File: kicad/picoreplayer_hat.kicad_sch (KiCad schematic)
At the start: 20 parts, among them J1 5v IN, J2 PANEL ON/OFF, J3 Raspberry_Pi3, J4 DISPLAY, J5 DAC, J6 PICORE ENCODER & BTN, K2 Relay_HFD2_bistabile, Q1 2N3904, Q2 2N3904, SW1 ON/OFF, SW2 HARD STOP

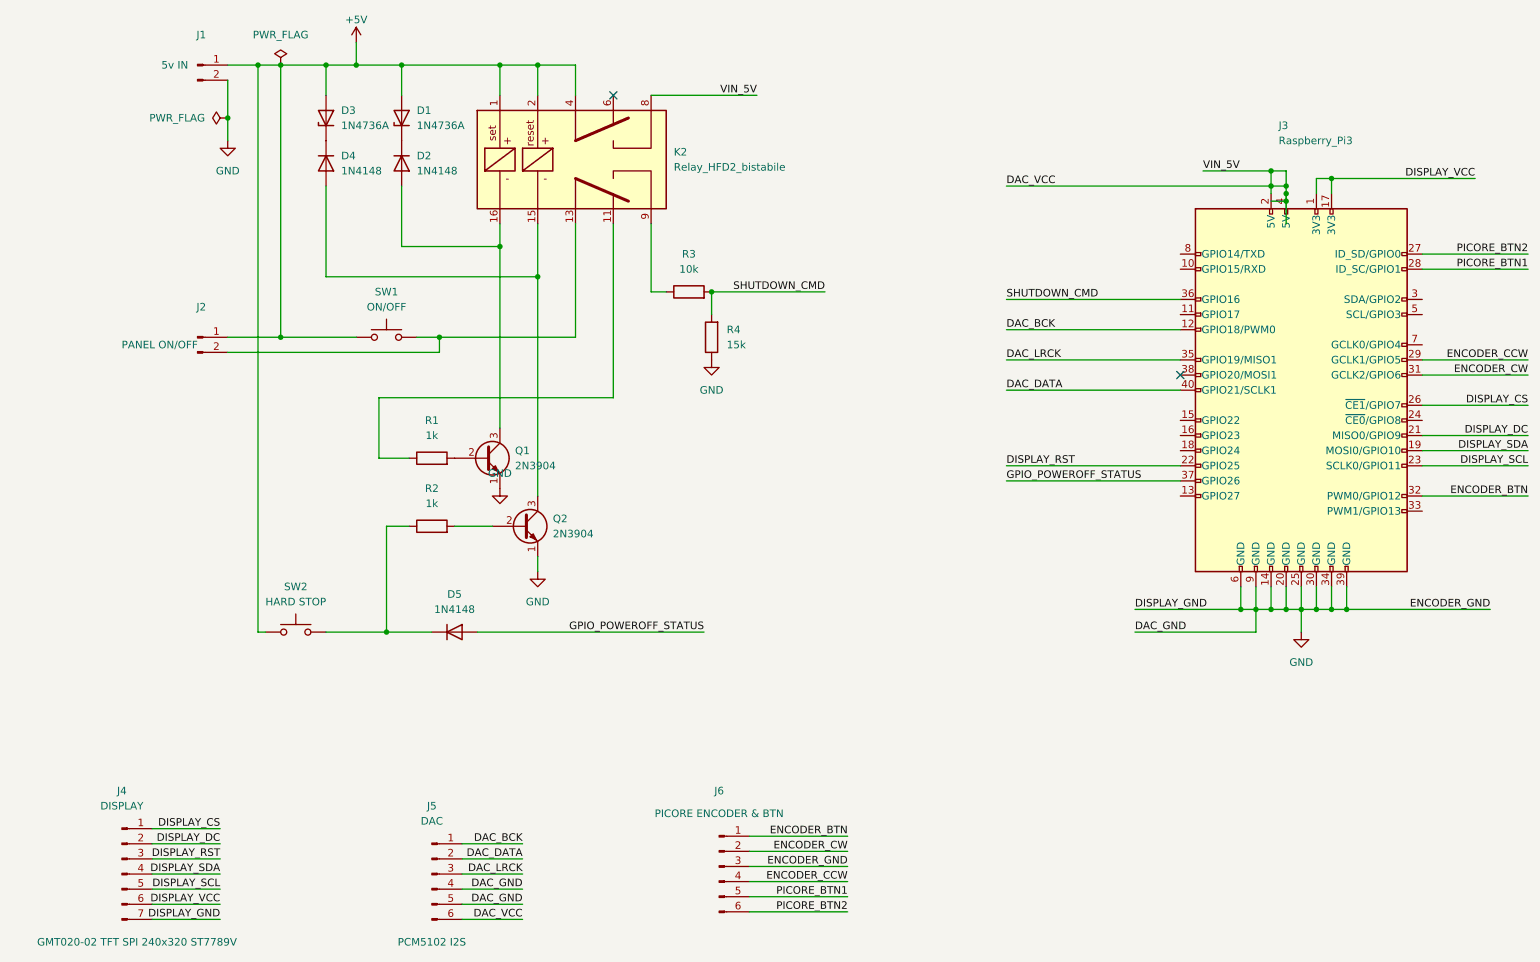
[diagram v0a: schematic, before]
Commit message: changed diode model to 1N4007 and added pulldown resistors to the transistor base
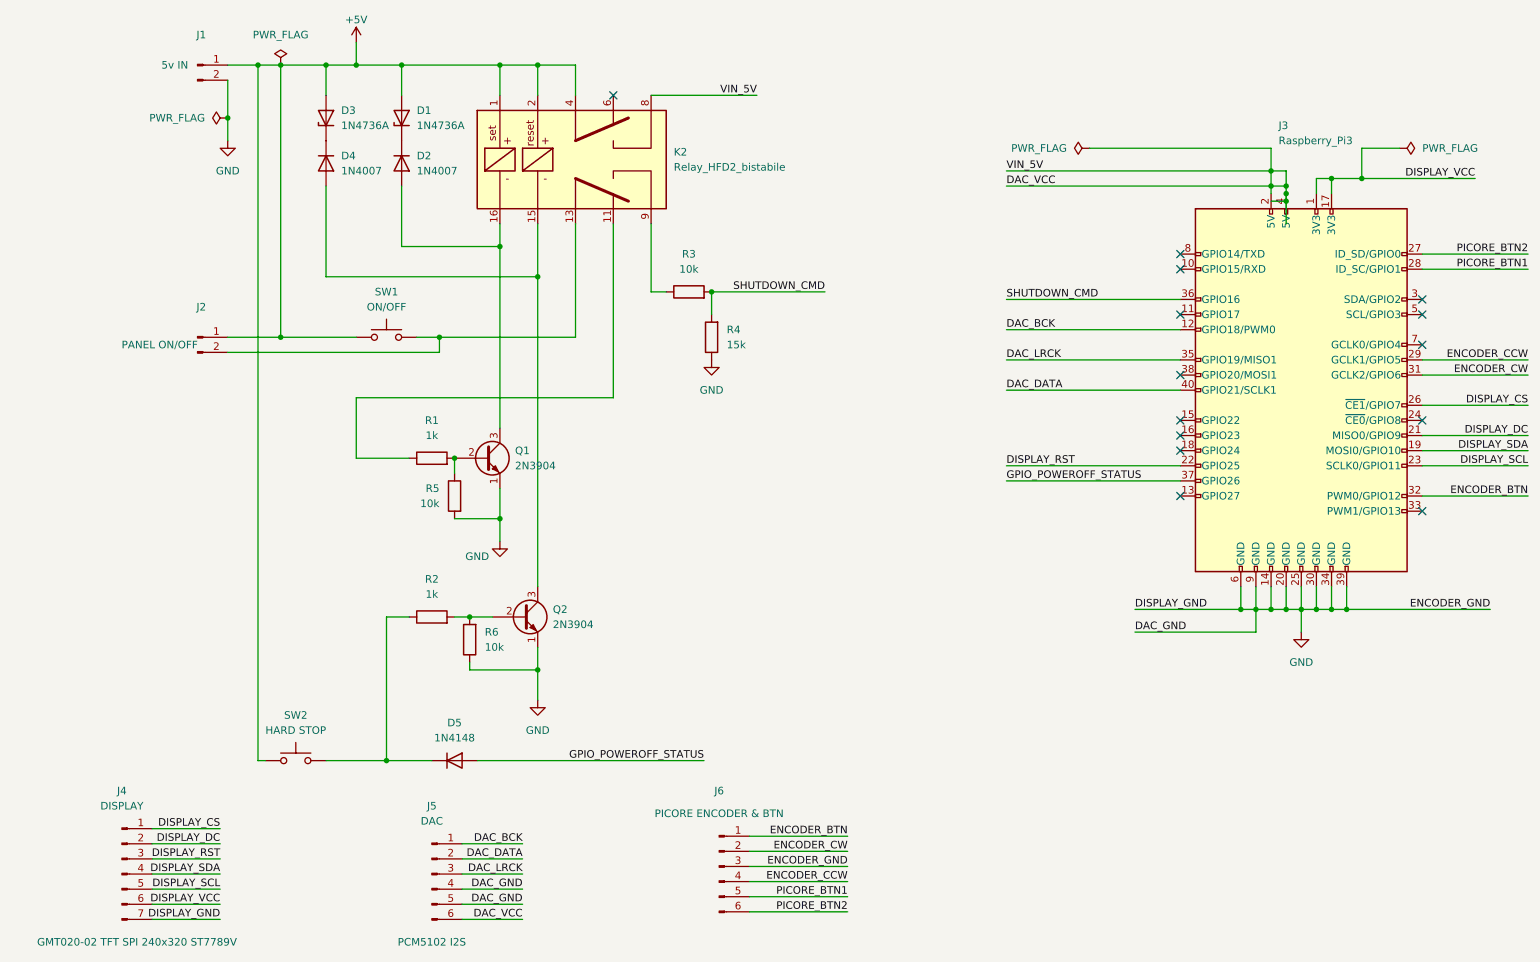
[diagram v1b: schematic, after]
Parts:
- added R5, R6: 10k, Resistor_THT:R_Axial_DIN0207_L6.3mm_D2.5mm_P7.62mm_Horizontal, symbol Device:R
- D2, D4: value 1N4148 -> 1N4007
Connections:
- net GND: now also R5.2, R6.1
- net at Q2.2 (B), R2.2: now also R6.2
- net at Q1.2 (B), R1.2: now also R5.1
- no-connect marks 2 -> 14
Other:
- moved on the sheet: D5, Q2, R2, SW2

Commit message: changed symbols and footprint for 1N4007
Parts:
- D2, D4: footprint Diode_THT:D_DO-35_SOD27_P7.62mm_Horizontal -> Diode_THT:D_DO-41_SOD81_P10.16mm_Horizontal; symbol Diode:1N4148 -> Diode:1N4007
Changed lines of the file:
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@@
     (title "piCore Hat")
     (date "2024-02-08")
-    (rev "1.0.0")
+    (rev "1.0.1")
     (company "Ivan Tarozzi")
     (comment 2 "itarozzi@gmail.com")
@@
     )
   )
-  (symbol (lib_id "Diode:1N4148") (at 80.01 48.26 270) (unit 1)
+  (symbol (lib_id "Diode:1N4007") (at 80.01 48.26 270) (unit 1)
     (in_bom yes) (on_board yes) (dnp no) (fields_autoplaced)
     (property "Reference" "D2" (at 82.55 46.99 90)
@@
       (effects (font (size 1.27 1.27)) (justify left))
     )
-    (property "Footprint" "Diode_THT:D_DO-35_SOD27_P7.62mm_Horizontal" (at 80.01 48.26 0)
-      (effects (font (size 1.27 1.27)) hide)
-    )
-    (property "Datasheet" "https://assets.nexperia.com/documents/data-sheet/1N4148_1N4448.pdf" (at 80.01 48.26 0)
+    (property "Footprint" "Diode_THT:D_DO-41_SOD81_P10.16mm_Horizontal" (at 75.565 48.26 0)
+      (effects (font (size 1.27 1.27)) hide)
+    )
+    (property "Datasheet" "http://www.vishay.com/docs/88503/1n4001.pdf" (at 80.01 48.26 0)
       (effects (font (size 1.27 1.27)) hide)
     )
@@
     )
   )
-  (symbol (lib_id "Diode:1N4148") (at 67.31 48.26 270) (unit 1)
+  (symbol (lib_id "Diode:1N4007") (at 67.31 48.26 270) (unit 1)
     (in_bom yes) (on_board yes) (dnp no) (fields_autoplaced)
     (property "Reference" "D4" (at 69.85 46.99 90)
@@
       (effects (font (size 1.27 1.27)) (justify left))
     )
-    (property "Footprint" "Diode_THT:D_DO-35_SOD27_P7.62mm_Horizontal" (at 67.31 48.26 0)
-      (effects (font (size 1.27 1.27)) hide)
-    )
-    (property "Datasheet" "https://assets.nexperia.com/documents/data-sheet/1N4148_1N4448.pdf" (at 67.31 48.26 0)
-      (effects (font (size 1.27 1.27)) hide)
-    )
+    (property "Footprint" "Diode_THT:D_DO-41_SOD81_P10.16mm_Horizontal" (at 62.865 48.26 0)
+      (effects (font (size 1.27 1.27)) hide)
+    )
+    (property "Datasheet" "http://www.vishay.com/docs/88503/1n4001.pdf" (at 67.31 48.26 0)
+      (effects (font (size 1.27 1.27)) hide)
+    )
